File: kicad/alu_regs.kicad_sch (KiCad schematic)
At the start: 10 parts, among them U19 SN74F377AN, U20 SN74F377AN, U21 SN74F377AN, U5 ATF22V10C-7PX, U6 ATF22V10C-7PX

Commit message: BOM/schematic: stocked substitutes from the first parts order
D18 Kingbright WP7113ID (LTL2R3KRD-EM out of stock), 100n TDK
FG28X7R1H104KNT00 (KEMET C320C104 $0.66 at Mouser), C45 TDK
FG24C0G1H153JNT06 (KEMET non-stocked), Vishay BAT85S-TAP and
1N4148-TAP, MF-RG300-0, USB4125-GF-A-0190; Mouser prices re-checked.

Co-Authored-By: Claude Opus 5.5 (1M context) <noreply@anthropic.com>
Claude-Session: https://claude.ai/code/session_017y5UgjExE8oeP7QrfvhCzb
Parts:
- C19, C20, C21, C5, C6: MPN C320C104K5R5TA -> FG28X7R1H104KNT00; Manufacturer KEMET -> TDK

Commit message: Put every symbol, footprint and 3D model in the project library
- gen_kicad_stock_footprints.py: copies of the KiCad 9.0.6 footprints the
  boards use (C_Disc, CP_Radial, DO-15/DO-35, LED, pin header, oscillator,
  TO-92, SIP9, mounting holes, net tie) into placard.pretty, and KiCad's
  STEP models for them and for the DIP socket / resistor kit footprints
  into placard.3dshapes
- model paths use the PLACARD_LIB text variable (main board
  ${KIPRJMOD}/lib, cartridges ${KIPRJMOD}/../lib) so the shared footprints
  find their models in all three projects
- placard_std gains the 28C256 EEPROM and the power symbols; symbol
  Footprint defaults name placard footprints (relay, SIP9, oscillator,
  TO-92, EEPROM socket)
- schematics regenerated with placard_std power/EEPROM symbols and
  placard: footprints; BOM CSVs and PDFs regenerated
- cartridge .kicad_pro files take in Justin's local KiCad 9 settings

Co-Authored-By: Claude Opus 5.5 <noreply@anthropic.com>
Claude-Session: https://claude.ai/code/session_017okF1JiLRNFTfH7Az85hff
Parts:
- C19, C20, C21, C5, C6: footprint Capacitor_THT:C_Disc_D5.0mm_W2.5mm_P5.00mm -> placard:C_Disc_D5.0mm_W2.5mm_P5.00mm

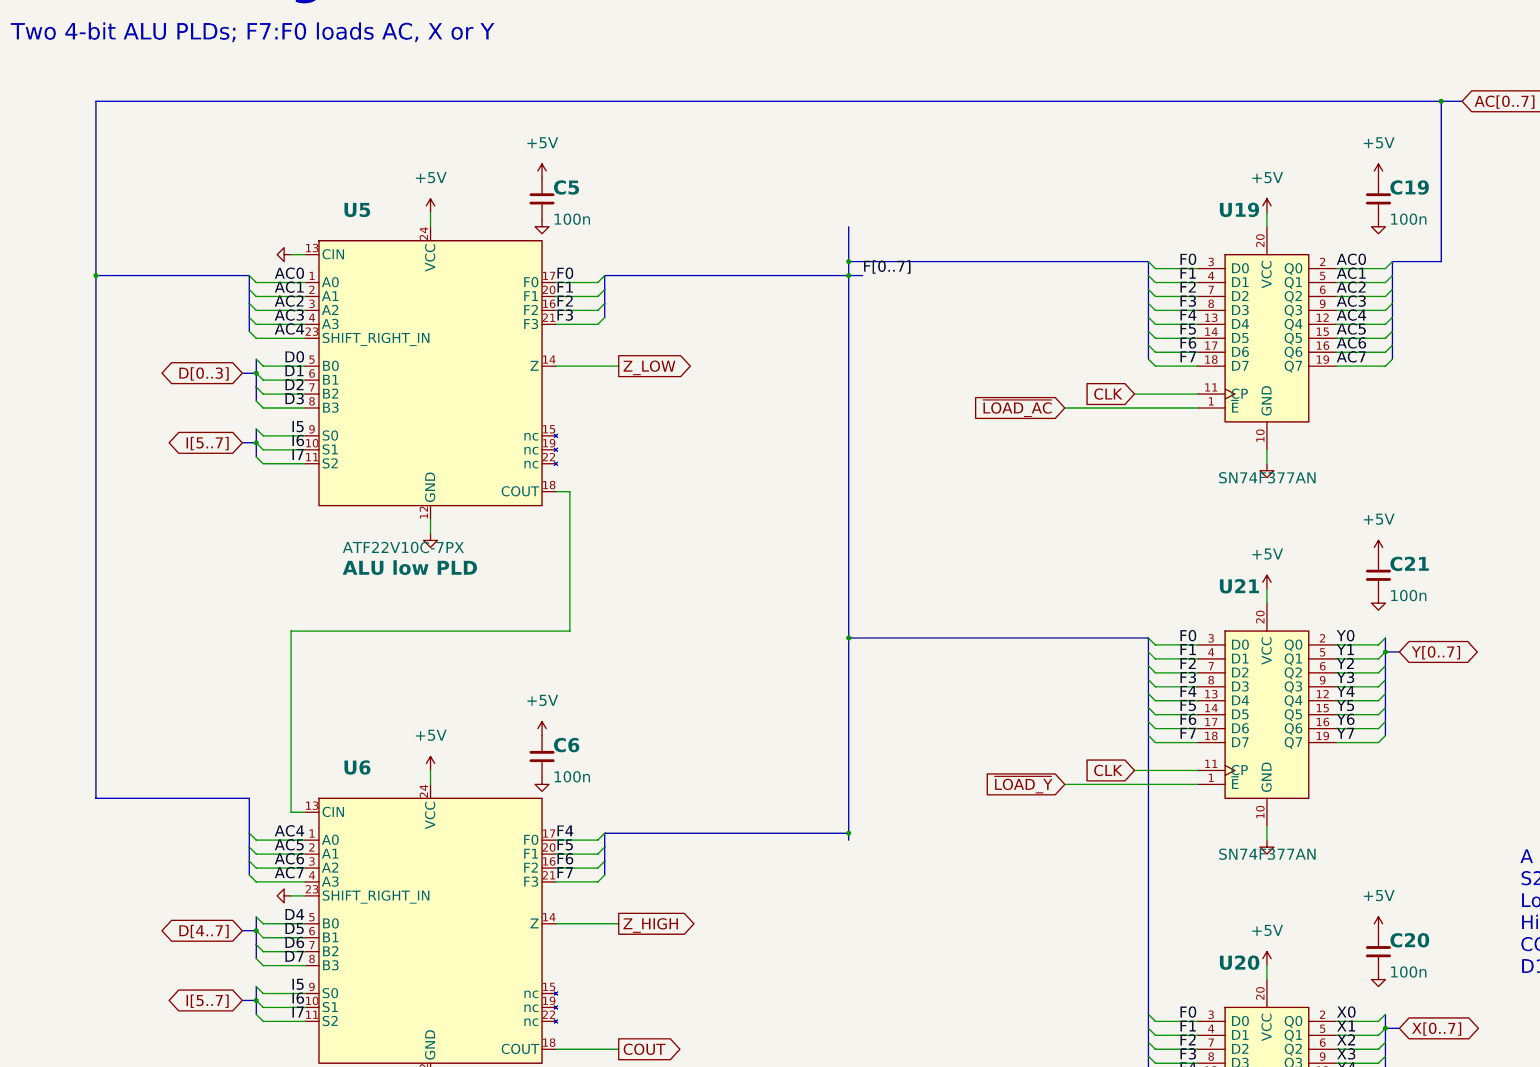
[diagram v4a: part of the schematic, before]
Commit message: Schematic: rename buses to ADDR / DATABUS / D, wire the shared port outputs
- Address bus A15:A0 is now ADDR15:ADDR0, the data bus D7:D0 is DATABUS7:DATABUS0
  and the D register's outputs DR7:DR0 are D7:D0 (main board and both cartridges).
- Shared port sheet: U38's outputs P_SCK, P_MOSI, P_CS, P_PS2D and K0 are wired
  to the SNES pads, the SD dividers and the PS/2 hold diodes (K0 -> D6 ->
  keyboard CLK).  J3 now sits level with U38's SCK/MOSI pins, J2 above it.
- Parts moved so the longer labels fit: U3/U4 and the PC bus, U18, U22, U11,
  U31, U32, RN1, R5-R12; expansion slots in two rows.
- SCHEMATIC_PLAN.md: the bus names.

Co-Authored-By: Claude Opus 5.5 <noreply@anthropic.com>
Claude-Session: https://claude.ai/code/session_01DnW5SUv7E4nz9tGtPvD1qV
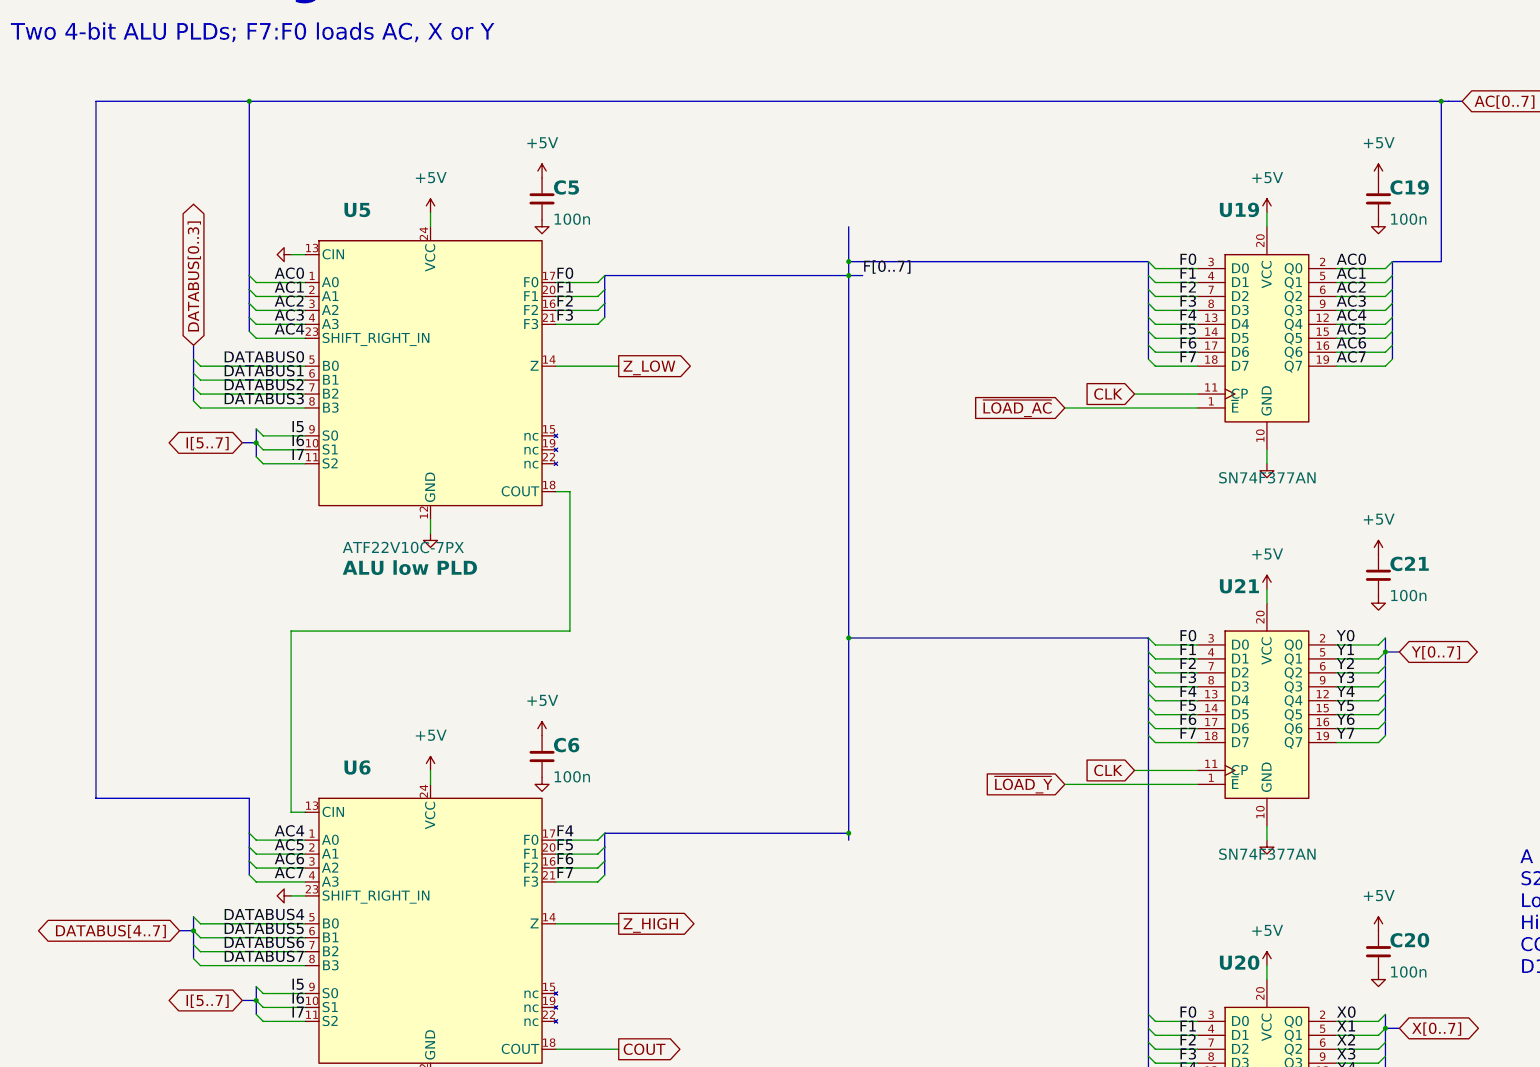
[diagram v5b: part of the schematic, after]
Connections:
- net D0 renamed DATABUS0
- net D1 renamed DATABUS1
- net D2 renamed DATABUS2
- net D3 renamed DATABUS3
- net D4 renamed DATABUS4
- net D5 renamed DATABUS5
- net D6 renamed DATABUS6
- net D7 renamed DATABUS7
